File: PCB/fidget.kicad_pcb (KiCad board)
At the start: 2 copper layers, 80.5 x 73.5 mm, 88 parts, among them J1 KEYSTONE 120, J2 KEYSTONE 120, U1 MCP73831-2ACI/MC, U10 SLG46140, U2 ESP8285, U3 TLV70033DSE, U4 LIS2DE, U5 TPS60150, U6 TPS60150, U7 TPS60150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

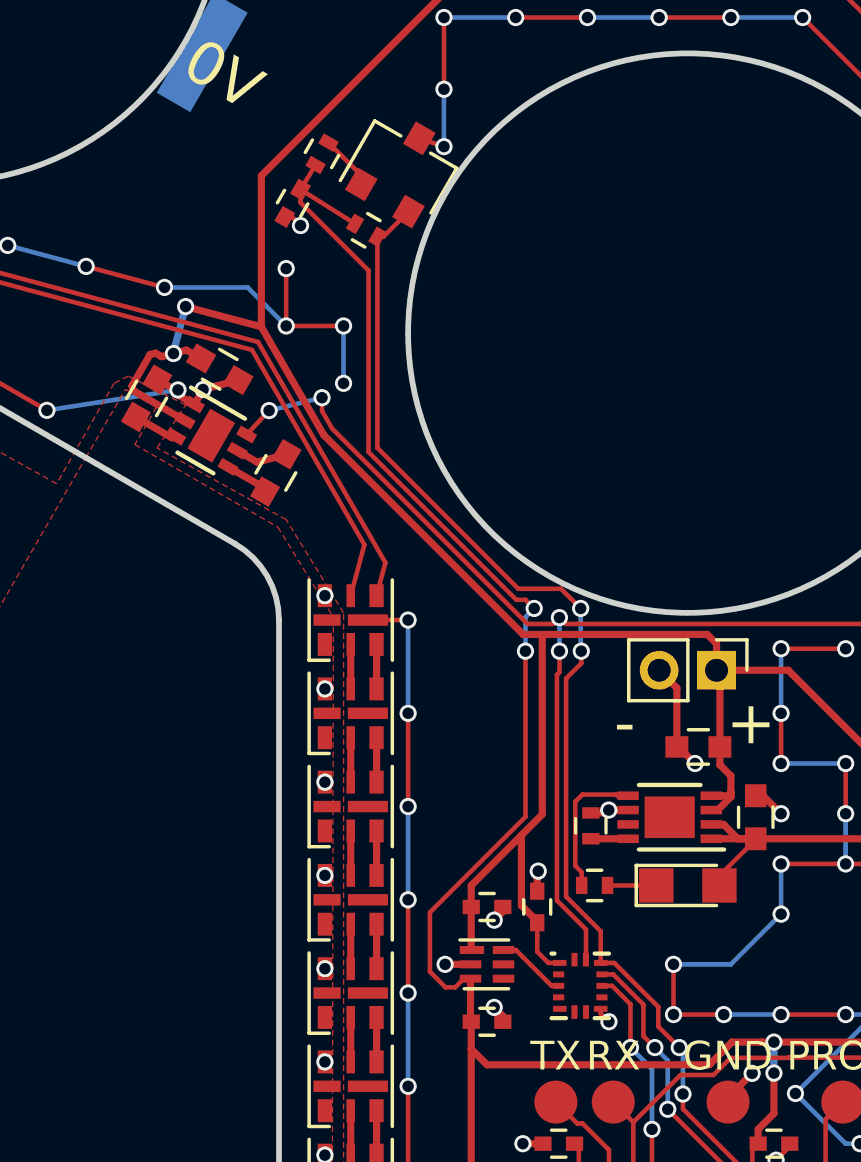
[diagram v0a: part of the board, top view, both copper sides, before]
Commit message: moved hall sensor to battery rail so it can work with the LDO powered off
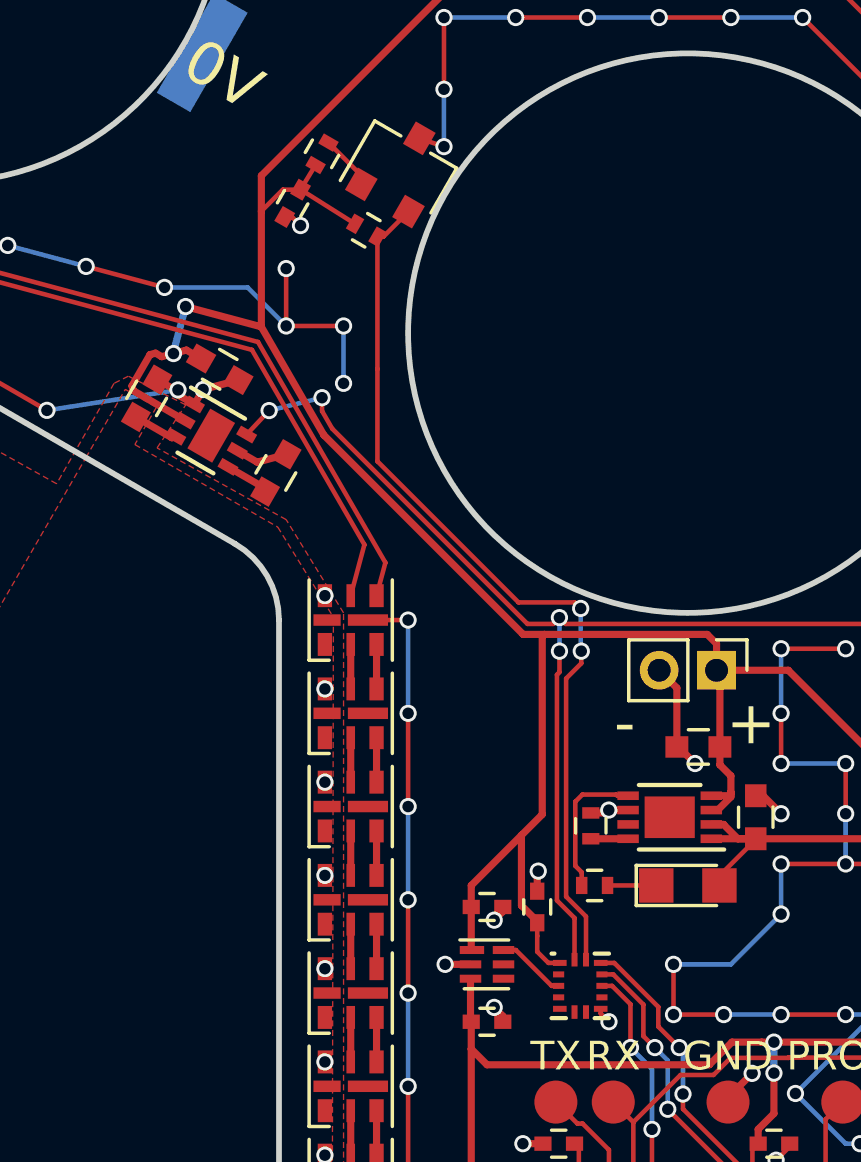
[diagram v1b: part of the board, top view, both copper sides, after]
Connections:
- C23 pad 1: +3V3 -> +BATT
- R14 pad 2: +3V3 -> +BATT
- R15 pad 1: +3V3 -> +BATT
- R15 pad 2: /IDX -> /IDX1
- U10 pad 13: /ENL -> /IDX1
- U10 pad 14: (no net) -> /ENL
- U8 pad 2: /IDX -> /IDX1
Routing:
- net +3V3: track 130.4 -> 93.3 mm, vias 8 -> 6
- net /IDX: track 41.0 -> 9.66 mm, vias 4 -> 2
- net /IDX1: track 0.00 -> 31.2 mm, vias 0 -> 2
- net +BATT: track 141.3 -> 146.2 mm

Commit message: added text to silkscreen
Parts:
- moved G2 24.1 mm to (87.5, 61.8)
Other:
- board text added: "bit.ly/2sj81Ge"
- board text added: "© 2017 Matthias Breithaupt"
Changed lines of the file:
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@@
     (area 59.669237 40.649999 140.330763 114.350001)
     (thickness 1.6)
-    (drawings 25)
+    (drawings 27)
     (tracks 960)
     (zones 0)
@@
     (34 B.Paste user)
     (35 F.Paste user)
-    (36 B.SilkS user hide)
+    (36 B.SilkS user)
     (37 F.SilkS user)
     (38 B.Mask user)
@@
     (visible_elements FFFFFF7F)
     (pcbplotparams
-      (layerselection 0x00030_80000001)
+      (layerselection 0x010fc_80000001)
       (usegerberextensions false)
       (excludeedgelayer true)
@@
       (outputformat 1)
       (mirror false)
-      (drillshape 1)
+      (drillshape 0)
       (scaleselection 1)
-      (outputdirectory ""))
+      (outputdirectory gerber/))
   )
   (net 0 "")
@@
     )
   )
-  (module Symbols:OSHW-Logo_7.5x8mm_SilkScreen locked (layer B.Cu)
-    (at 93 85.2 180)
+  (module Symbols:OSHW-Logo_7.5x8mm_SilkScreen (layer B.Cu)
+    (at 87.5 61.75 180)
     (descr "Open Source Hardware Logo")
     (tags "Logo OSHW")
@@
     )
   )
+  (gr_text bit.ly/2sj81Ge (at 100 109.25) (layer F.SilkS)
+    (effects (font (size 1 1) (thickness 0.15)))
+  )
+  (gr_text "© 2017\nMatthias Breithaupt" (at 100 109.75 360) (layer B.SilkS)
+    (effects (font (size 1 1) (thickness 0.15)) (justify mirror))
+  )
   (gr_text 0V (at 83.8 61 330) (layer F.SilkS)

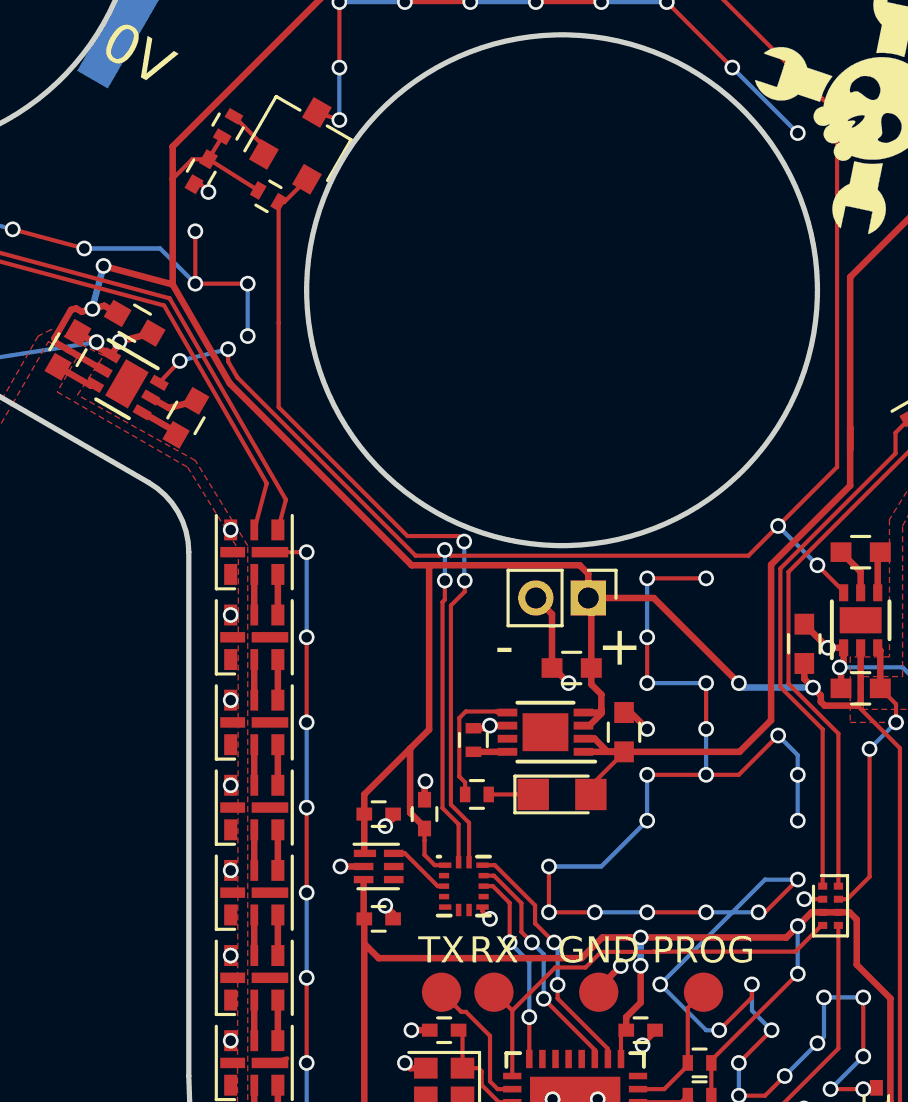
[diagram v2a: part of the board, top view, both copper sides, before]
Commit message: control power to hall sensor from pld
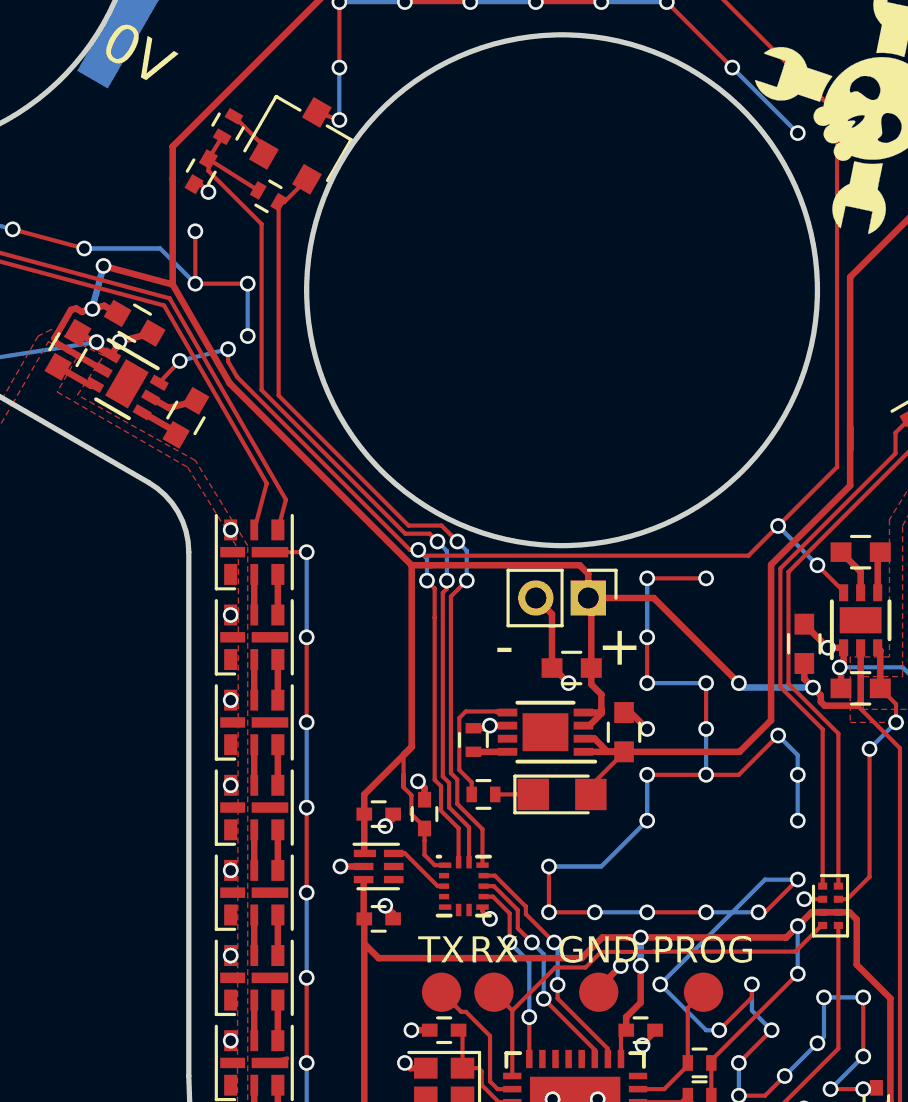
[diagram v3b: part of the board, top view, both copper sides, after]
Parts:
- moved R1 0.25 mm to (97.0, 89.2)
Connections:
- C23 pad 1: +BATT -> /TLV
- R14 pad 2: +BATT -> /TLV
- R15 pad 1: +BATT -> /TLV
- U10 pad 10: /LDO1 -> /ENL1
- U10 pad 11: /ENL1 -> /IDX
- U10 pad 12: /IDX -> /IDX1
- U10 pad 13: /IDX1 -> /TLV
- U10 pad 9: (no net) -> /LDO1
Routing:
- net /TLV: track 0.00 -> 34.9 mm, vias 0 -> 2
- net +BATT: track 146.2 -> 141.6 mm

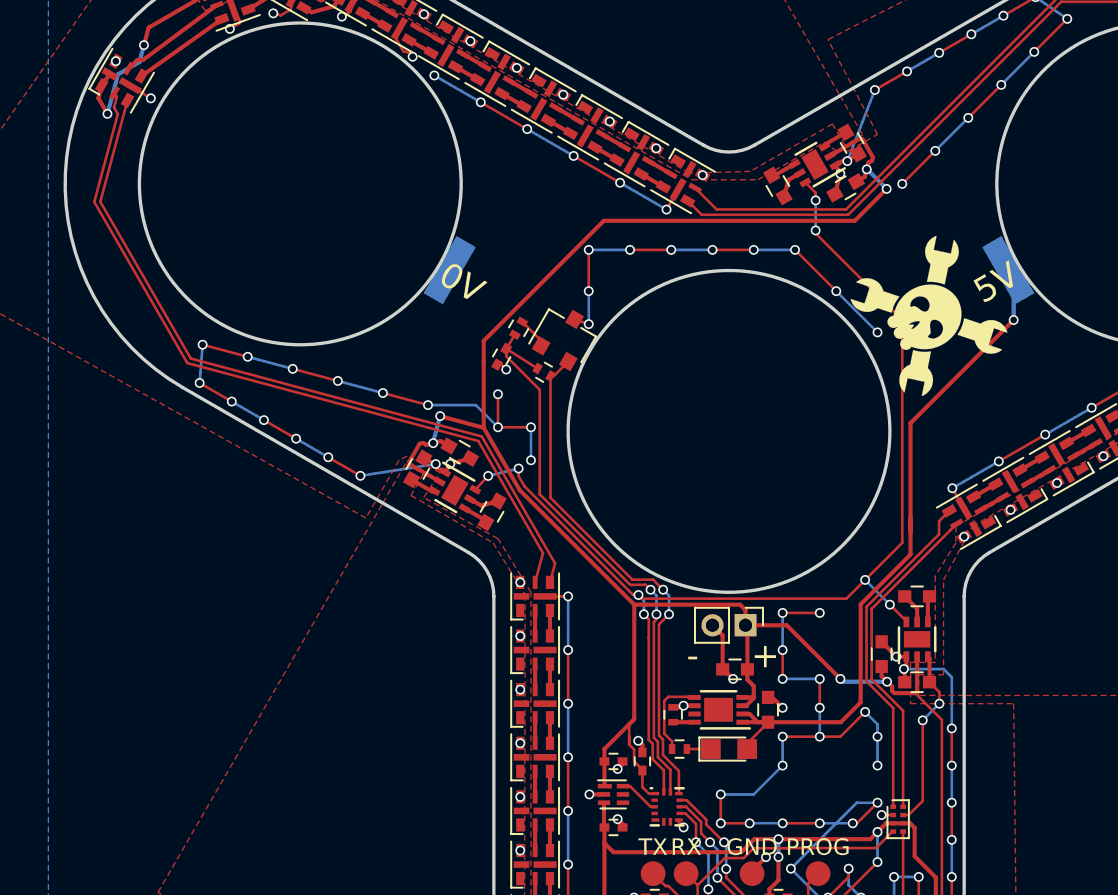
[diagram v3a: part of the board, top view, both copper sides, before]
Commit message: increase center hole to 608 size - outer bearings are still 626
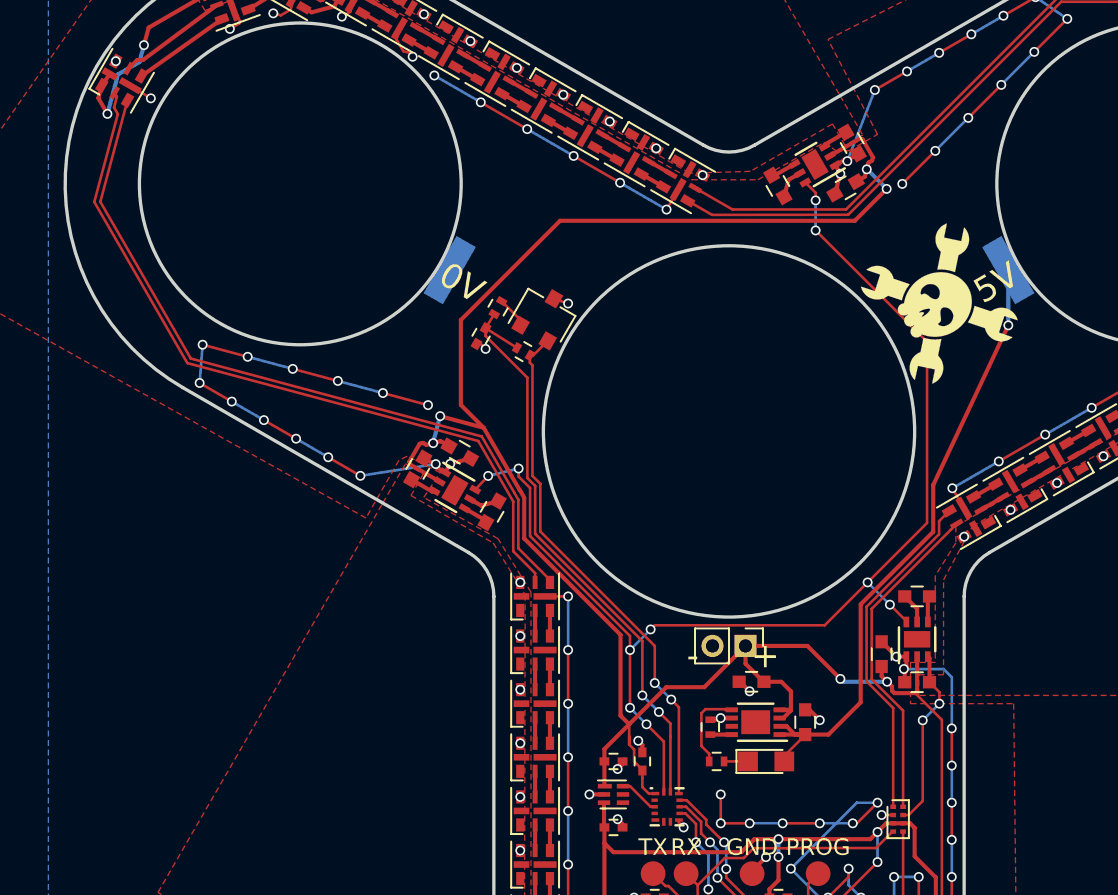
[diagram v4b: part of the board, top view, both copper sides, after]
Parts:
- moved C1 2.37 mm to (104.6, 87.6)
- moved D33 2.37 mm to (102.2, 90.0)
- moved R1 2.37 mm to (99.2, 90.0)
- moved R2 2.37 mm to (98.9, 87.9)
- moved U1 2.37 mm to (101.6, 87.6)
- moved C23 1.77 mm to (85.0, 64.2)
- moved R14 1.77 mm to (86.0, 62.5)
- moved R15 1.77 mm to (87.5, 65.2)
- moved U8 1.77 mm to (88.8, 63.0)
- moved BT1 1.25 mm to (101.0, 83.0)
- moved C2 1.25 mm to (101.4, 85.2)
- moved G1 0.98 mm to (112.8, 62.2)
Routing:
- net GND: track 327.1 -> 261.9 mm, vias 182 -> 157
- net +BATT: track 141.6 -> 145.5 mm
- net +5V: track 42.6 -> 38.7 mm
- net /ENL: track 71.7 -> 74.5 mm, vias 8 -> 10
- net /TLV: track 34.9 -> 36.0 mm
- net /IDX1: track 31.2 -> 31.7 mm
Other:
- outline, holes or cut-outs redrawn

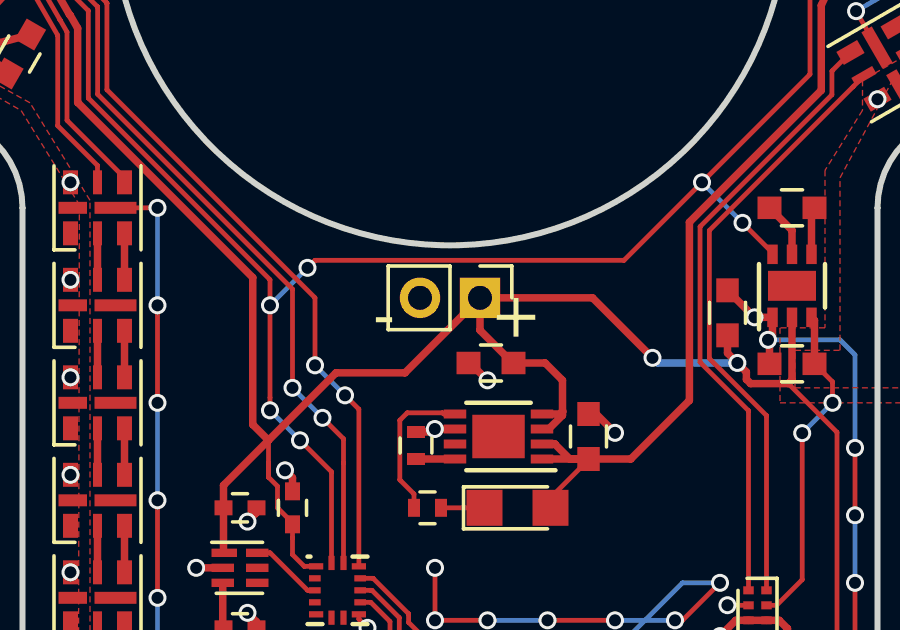
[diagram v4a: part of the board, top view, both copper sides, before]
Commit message: fixed silkscreen
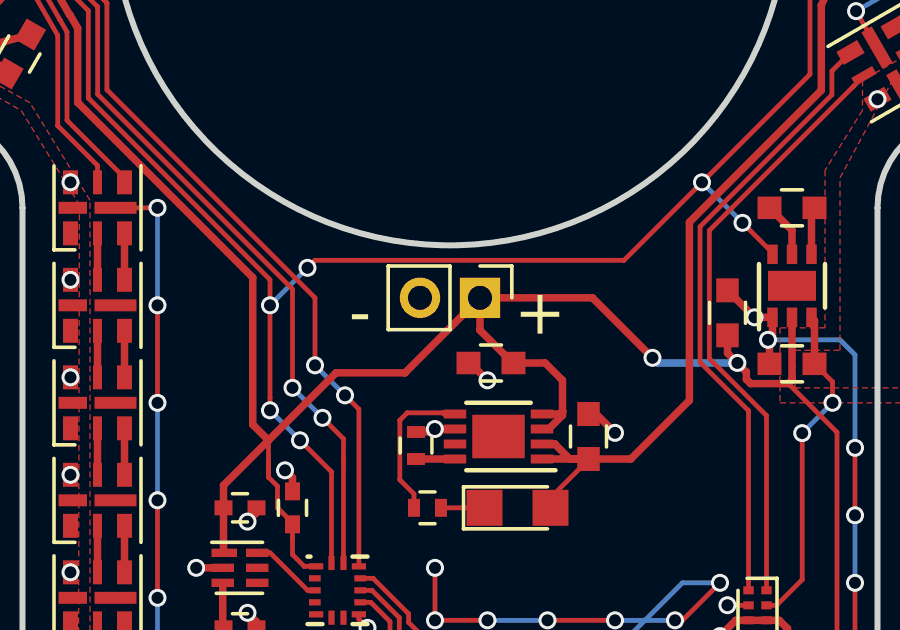
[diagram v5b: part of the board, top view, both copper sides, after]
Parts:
- moved G2 4.83 mm to (89.2, 57.2)
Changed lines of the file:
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@@
   )
   (setup
-    (last_trace_width 0.16)
+    (last_trace_width 0.25)
     (user_trace_width 0.16)
     (user_trace_width 0.2)
@@
   )
   (module Symbols:OSHW-Logo_7.5x8mm_SilkScreen (layer B.Cu)
-    (at 87.5 61.75 180)
+    (at 89.25 57.25 180)
     (descr "Open Source Hardware Logo")
     (tags "Logo OSHW")
@@
     (effects (font (size 1.5 1.5) (thickness 0.3)))
   )
-  (gr_text - (at 97.8 83.6) (layer F.SilkS)
+  (gr_text - (at 97 83.5) (layer F.SilkS)
     (effects (font (size 1.5 1.5) (thickness 0.3)))
   )
-  (gr_text + (at 102.2 83.6) (layer F.SilkS)
+  (gr_text + (at 103 83.5) (layer F.SilkS)
     (effects (font (size 1.5 1.5) (thickness 0.3)))
   )
